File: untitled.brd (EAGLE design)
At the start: 100 x 80 mm, 31 parts, among them IC1 STM8S003F3

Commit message: second commit
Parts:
- added TP15: TPB2,54, testpad:B2,54
- moved SWIM 34.9 mm to (38.7, 11.7)
- moved TP13 29.6 mm to (27.3, 9.21)
- moved TP14 29.4 mm to (22.9, 9.21)
- moved C5 26.9 mm to (44.1, 15.6)
- moved IC1 24.5 mm to (38.7, 18.1)
- moved TP4 20.6 mm to (45.4, 24.1)
- moved TP3 20.3 mm to (45.4, 27.6)
- moved C2 11.1 mm to (38.1, 26.6)
- moved C4 11.1 mm to (40.3, 24.7)
- moved L1 11.1 mm to (42.5, 24.4)
- moved R4 11.1 mm to (37.1, 23.7)
- moved C3 11.1 mm to (41.3, 27.6)
- moved TP8 10.9 mm to (36.2, 30.8)
- moved TP6 9.74 mm to (36.2, 34.6)
- moved TP7 9.10 mm to (40.0, 30.8)
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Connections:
- removed net N$25: C1.2, C5.2, IC1.7, SWIM.3
- new net N$1: IC1.14, TP15.TP
- net GND: now also C1.2, C5.2, IC1.7, SWIM.3
- net NEXT: now also IC1.17; no longer IC1.1
- net PLAY_PAUSE: now also IC1.20; no longer IC1.3
- net PRE: now also IC1.19; no longer IC1.2
- net VOL+: now also IC1.15; no longer IC1.19
- net VOL-: now also IC1.16; no longer IC1.20
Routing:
- net LED0: track 48.8 -> 4.59 mm
- net VCC: track 43.8 -> 85.5 mm
- net VOL+: track 45.2 -> 5.72 mm
- net VOL-: track 41.7 -> 5.52 mm
- net PLAY_PAUSE: track 31.6 -> 4.76 mm
- net PRE: track 27.3 -> 5.41 mm
- net GND: track 77.5 -> 57.8 mm
- net NEXT: track 22.9 -> 5.33 mm
- net N$26: track 3.97 -> 9.89 mm
- net N$18: track 7.21 -> 12.6 mm
- net N$28: track 10.6 -> 6.02 mm
- net N$16: track 9.52 -> 14.0 mm
- net N$10: track 4.50 -> 8.57 mm
- net N$9: track 7.07 -> 11.1 mm
- net N$25: track 3.95 -> 0.00 mm
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
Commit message: third commit
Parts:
- removed TP1, TP2: TPB2,54, testpad:B2,54
- added SWIM1: (no value), con-lstb:MA04-1
- added U$2: MCP1825SOT-223-3, SteelCaveRobotics-Power:SOT-223
- LED1, LED2, LED3: device led:CHIP-LED0805 -> led:CHIPLED_0603
- moved TP11 7.73 mm to (12.4, 20.3)
- moved TP9 7.62 mm to (12.7, 25.4)
- moved TP13 7.31 mm to (20.0, 8.89)
- moved TP12 6.70 mm to (10.8, 17.5)
- moved TP10 5.85 mm to (10.8, 22.9)
- moved R5 5.75 mm to (15.2, 16.5)
- moved LED1 4.49 mm to (13.3, 32.4)
- moved TP15 4.46 mm to (47.9, 15.6)
- moved LED3 3.24 mm to (13.3, 29.8)
- moved TP14 2.88 mm to (25.7, 8.89)
- moved TP6 1.59 mm to (37.8, 34.6)
- moved TP8 1.59 mm to (37.8, 30.8)
- moved TP5 1.27 mm to (41.3, 34.6)
- moved TP7 1.27 mm to (41.3, 30.8)
- moved LED2 0.90 mm to (13.3, 31.1)
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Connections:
- removed net N$13: TP1.TP, U$1.P$10
- removed net N$14: TP2.TP, U$1.P$11
- new net VDD: TP13.TP, U$2.1
- net GND: now also U$2.2
- net LED0: now also LED3.C; no longer LED1.C
- net LED2: now also LED1.C; no longer LED3.C
- net N$1: now also IC1.3; no longer IC1.14
- net N$20: now also SWIM1.1
- net N$21: now also SWIM1.2
- net N$22: now also SWIM1.3
- net N$23: now also SWIM1.4
- net N$4: now also LED1.A; no longer LED3.A
- net N$6: now also LED3.A; no longer LED1.A
- net VCC: now also U$2.3; no longer TP13.TP
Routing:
- net N$12: track 14.3 -> 2.48 mm
- net VCC: track 85.5 -> 74.2 mm
- net N$14: track 9.00 -> 0.00 mm, vias 0 -> 1
- net N$1: track 0.00 -> 6.67 mm
- net N$13: track 6.39 -> 0.00 mm, vias 0 -> 1
- net VDD: track 0.00 -> 5.56 mm
- net N$15: track 12.0 -> 7.16 mm
- net GND: track 57.8 -> 62.3 mm
- net N$23: track 18.6 -> 14.6 mm
- net N$22: track 16.8 -> 13.3 mm
- net N$21: track 14.5 -> 11.9 mm
- net N$20: track 13.4 -> 11.3 mm
- net N$19: track 6.40 -> 7.99 mm
- net N$16: track 14.0 -> 15.6 mm
- net N$6: track 1.81 -> 3.27 mm
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- added copper zone on layer 1, net GND

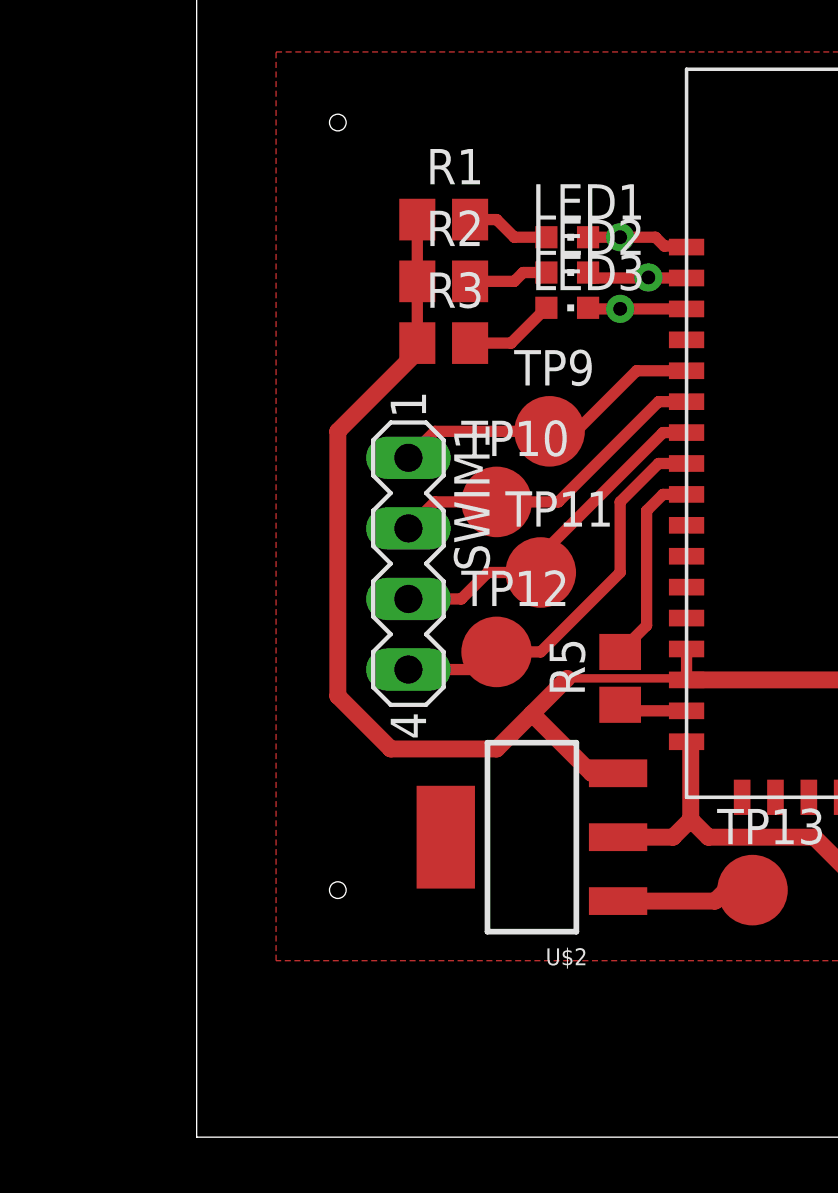
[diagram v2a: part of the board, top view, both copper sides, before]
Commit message: removed leds
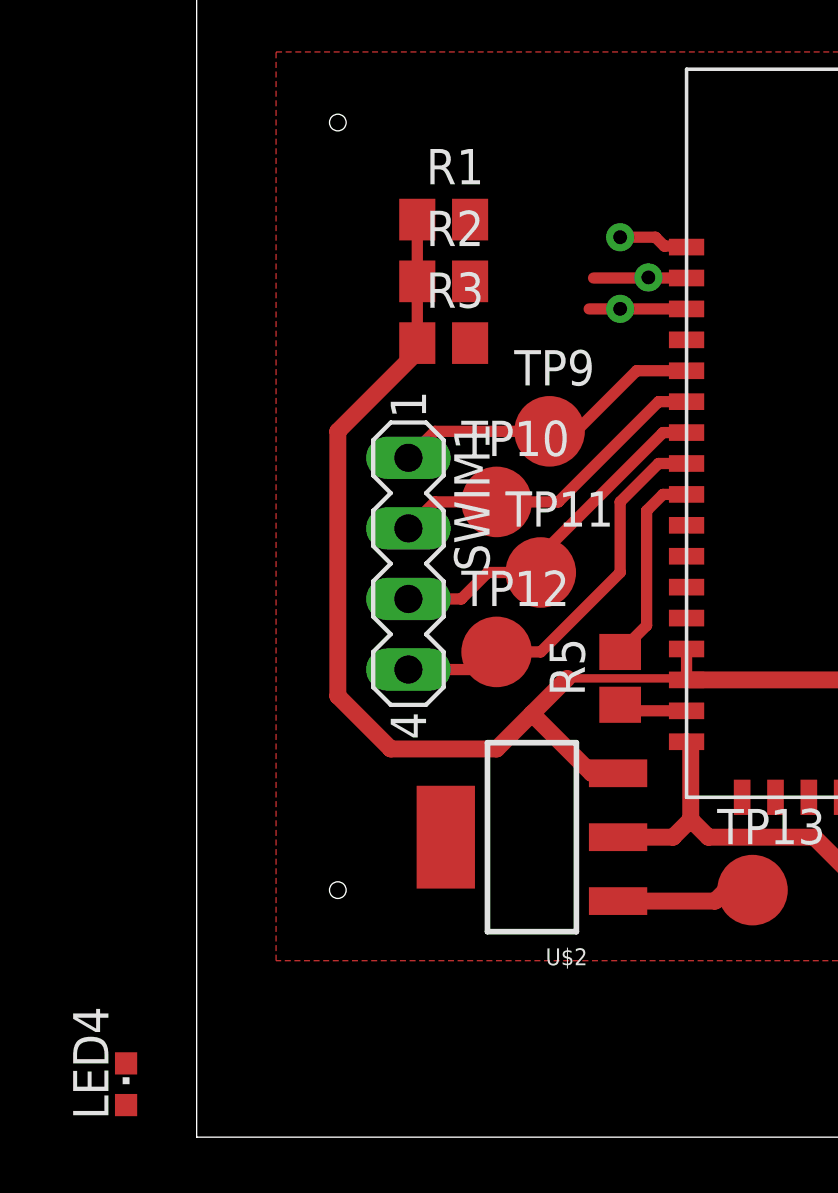
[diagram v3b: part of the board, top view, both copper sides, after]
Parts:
- removed LED1, LED2, LED3: (no value), led:CHIPLED_0603
- added LED4: (no value), led:CHIPLED_0603
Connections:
- removed net N$4: LED1.A, R1.2
- removed net N$5: LED2.A, R2.2
- removed net N$6: LED3.A, R3.2
- net LED0: now also R3.2; no longer LED3.C
- net LED1: now also R2.2; no longer LED2.C
- net LED2: now also R1.2; no longer LED1.C
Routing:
- net N$6: track 3.27 -> 0.00 mm
- net N$4: track 3.01 -> 0.00 mm
- net N$5: track 2.88 -> 0.00 mm
- net LED2: track 5.14 -> 3.98 mm
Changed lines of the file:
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@@
 <?xml version="1.0" encoding="utf-8"?>
 <!DOCTYPE eagle SYSTEM "eagle.dtd">
-<eagle version="7.3.0">
+<eagle version="7.4.0">
 <drawing>
 <settings>
@@
 <attribute name="OC_FARNELL" value="unknown" x="7.62" y="20.6375" size="1.778" layer="27" rot="R270" display="off"/>
 </element>
-<element name="LED1" library="led" package="CHIPLED_0603" value="" x="13.335" y="32.385" rot="R270"/>
-<element name="LED2" library="led" package="CHIPLED_0603" value="" x="13.335" y="31.115" rot="R270"/>
-<element name="LED3" library="led" package="CHIPLED_0603" value="" x="13.335" y="29.845" rot="R270"/>
 <element name="U$2" library="SteelCaveRobotics-Power" package="SOT-223" value="MCP1825SOT-223-3" x="12.065" y="10.795" rot="R90"/>
+<element name="LED4" library="led" package="CHIPLED_0603" value="" x="-2.54" y="1.905"/>
 </elements>
 <signals>
@@
 <wire x1="44.135" y1="18.415" x2="44.1325" y2="18.4175" width="0.4064" layer="1"/>
 </signal>
-<signal name="N$4">
-<contactref element="R1" pad="2"/>
-<contactref element="LED1" pad="A"/>
-<wire x1="12.585" y1="32.385" x2="11.43" y2="32.385" width="0.4064" layer="1"/>
-<wire x1="11.43" y1="32.385" x2="10.795" y2="33.02" width="0.4064" layer="1"/>
-<wire x1="10.795" y1="33.02" x2="9.84" y2="33.02" width="0.4064" layer="1"/>
-</signal>
-<signal name="N$5">
-<contactref element="R2" pad="2"/>
-<contactref element="LED2" pad="A"/>
-<wire x1="12.585" y1="31.115" x2="11.7475" y2="31.115" width="0.4064" layer="1"/>
-<wire x1="11.7475" y1="31.115" x2="11.43" y2="30.7975" width="0.4064" layer="1"/>
-<wire x1="11.43" y1="30.7975" x2="9.84" y2="30.7975" width="0.4064" layer="1"/>
-</signal>
-<signal name="N$6">
-<contactref element="R3" pad="2"/>
-<contactref element="LED3" pad="A"/>
-<wire x1="9.84" y1="28.575" x2="11.315" y2="28.575" width="0.4064" layer="1"/>
-<wire x1="11.315" y1="28.575" x2="12.585" y2="29.845" width="0.4064" layer="1"/>
-</signal>
 <signal name="VCC">
 <contactref element="R1" pad="1"/>
@@
 <contactref element="IC1" pad="10"/>
 <contactref element="U$1" pad="P$1"/>
-<contactref element="LED1" pad="C"/>
-<wire x1="14.085" y1="32.385" x2="15.24" y2="32.385" width="0.4064" layer="1"/>
 <wire x1="15.24" y1="32.385" x2="16.51" y2="32.385" width="0.4064" layer="1"/>
 <wire x1="16.51" y1="32.385" x2="16.8275" y2="32.0675" width="0.4064" layer="1"/>
@@
 <wire x1="41.6528" y1="21.0225" x2="42.295" y2="21.0225" width="0.4064" layer="1"/>
 <wire x1="42.295" y1="21.0225" x2="42.8625" y2="21.59" width="0.4064" layer="1"/>
+<contactref element="R1" pad="2"/>
 <wire x1="17.63" y1="32.03" x2="41.6528" y2="21.0225" width="0" layer="19" extent="1-1"/>
+<wire x1="9.84" y1="33.02" x2="15.24" y2="32.385" width="0" layer="19" extent="1-1"/>
 </signal>
 <signal name="LED1">
 <contactref element="IC1" pad="12"/>
 <contactref element="U$1" pad="P$2"/>
-<contactref element="LED2" pad="C"/>
 <wire x1="17.63" y1="30.9175" x2="14.2825" y2="30.9175" width="0.4064" layer="1"/>
-<wire x1="14.2825" y1="30.9175" x2="14.085" y2="31.115" width="0.4064" layer="1"/>
 <wire x1="35.8172" y1="20.3725" x2="34.8725" y2="20.3725" width="0.4064" layer="1"/>
 <wire x1="34.8725" y1="20.3725" x2="34.6075" y2="20.6375" width="0.4064" layer="1"/>
+<contactref element="R2" pad="2"/>
 <wire x1="17.63" y1="30.9175" x2="34.6075" y2="20.6375" width="0" layer="19" extent="1-1"/>
+<wire x1="9.84" y1="30.7975" x2="14.2825" y2="30.9175" width="0" layer="19" extent="1-1"/>
 </signal>
 <signal name="LED0">
 <contactref element="IC1" pad="11"/>
 <contactref element="U$1" pad="P$3"/>
-<contactref element="LED3" pad="C"/>
 <wire x1="17.63" y1="29.805" x2="14.125" y2="29.805" width="0.4064" layer="1"/>
-<wire x1="14.125" y1="29.805" x2="14.085" y2="29.845" width="0.4064" layer="1"/>
 <wire x1="35.8172" y1="21.0225" x2="35.4925" y2="21.0225" width="0.4064" layer="1"/>
 <wire x1="35.4925" y1="21.0225" x2="35.2425" y2="21.2725" width="0.4064" layer="1"/>
@@
 <wire x1="35.2425" y1="21.59" x2="35.56" y2="21.9075" width="0.4064" layer="1"/>
 <wire x1="35.56" y1="21.9075" x2="35.8775" y2="21.9075" width="0.4064" layer="1"/>
+<contactref element="R3" pad="2"/>
 <wire x1="17.63" y1="29.805" x2="35.2425" y2="21.59" width="0" layer="19" extent="1-1"/>
+<wire x1="9.84" y1="28.575" x2="14.125" y2="29.805" width="0" layer="19" extent="1-1"/>
 </signal>
 <signal name="N$1">

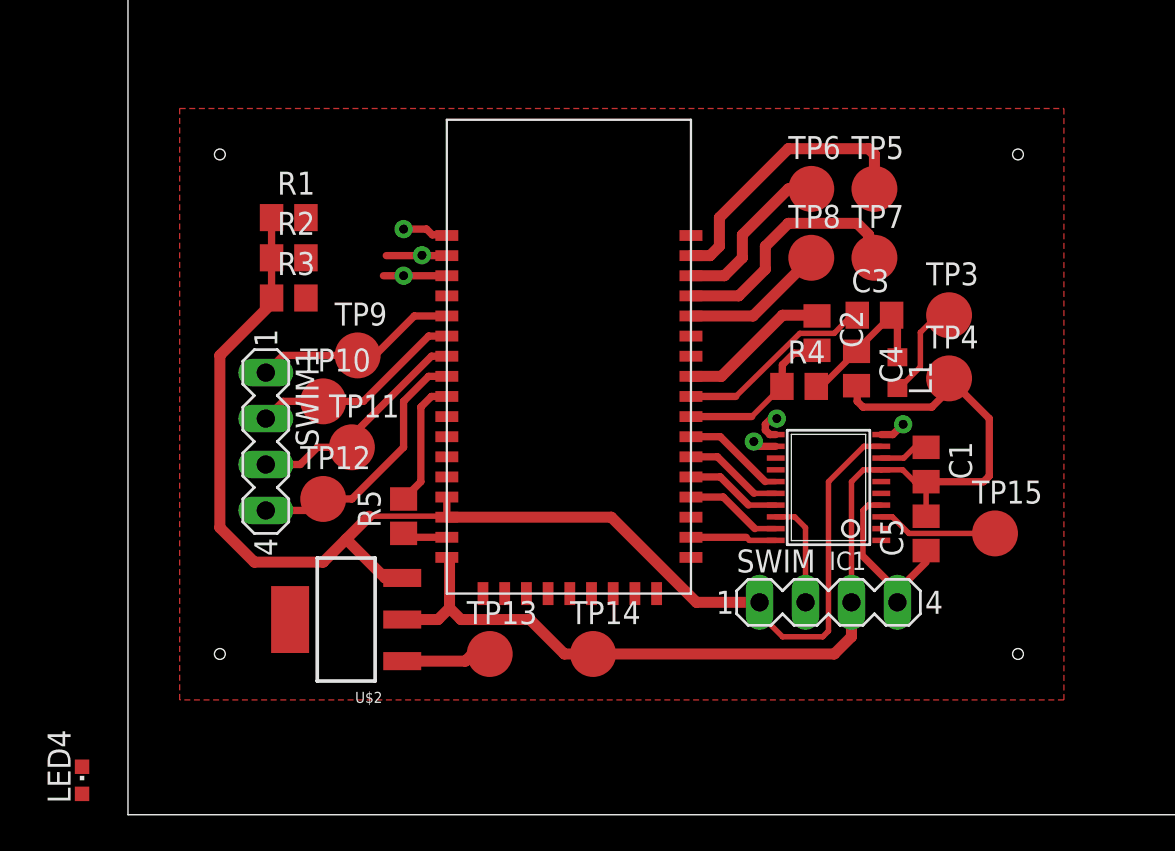
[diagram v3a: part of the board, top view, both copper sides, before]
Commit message: added tx signal + led
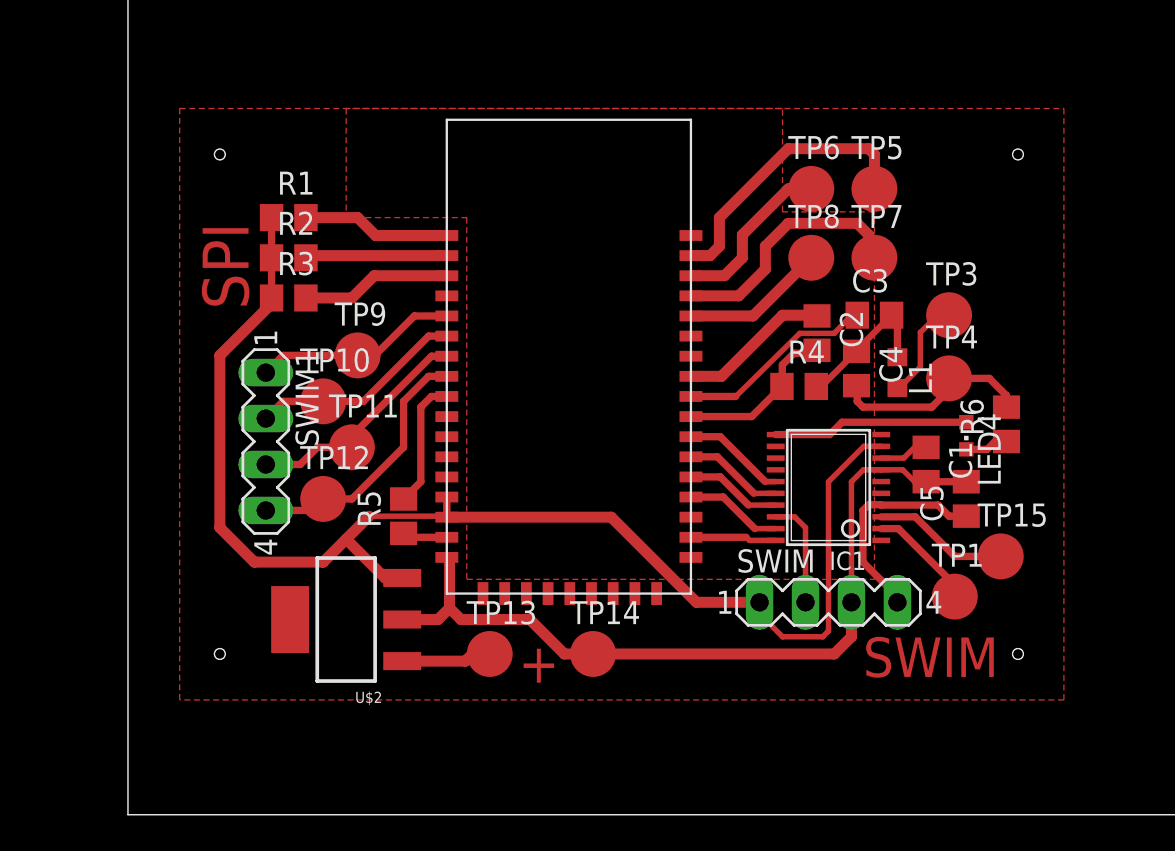
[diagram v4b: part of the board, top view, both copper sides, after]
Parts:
- added R6: 100, rcl:R0805
- added TP1: TPB2,54, testpad:B2,54
- moved LED4 52.5 mm to (46.4, 21.0), turned to 180 degrees
- moved C5 2.93 mm to (46.4, 17.5)
- moved TP15 1.31 mm to (48.3, 14.3)
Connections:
- new net N$29: LED4.C, R6.1
- new net N$5: IC1.2, TP1.TP
- new net N$6: IC1.11, LED4.A
- net GND: now also R6.2
- net LED0: now also IC1.10; no longer IC1.11
- net LED1: no longer IC1.12
- net LED2: no longer IC1.10
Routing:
- net N$6: track 0.00 -> 10.8 mm
- net N$5: track 0.00 -> 6.00 mm
- net GND: track 62.3 -> 57.3 mm
- net LED2: track 3.98 -> 8.20 mm, vias 1 -> 0
- net LED1: track 4.67 -> 7.84 mm
- net LED0: track 5.27 -> 8.30 mm
- net N$29: track 0.00 -> 2.40 mm
- net N$26: track 9.89 -> 12.0 mm
- net N$1: track 6.67 -> 7.51 mm
- added copper zone on layer 1, net N$4
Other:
- board text added: "+"
- board text added: "SPI"
- board text added: "SWIM"

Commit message: new design
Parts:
- removed TP10, TP11, TP12, TP9: TPB2,54, testpad:B2,54
- added C6, C7: 104, rcl:C0805
- added LED1: (no value), led:CHIPLED_0603
- added R10, R7, R8, R9: (no value), rcl:R0805
- moved SWIM1 0.71 mm to (7.94, 21.3)
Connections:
- new net N$30: R8.2, U$1.P$6
- new net N$31: R9.1, SWIM1.3
- new net N$32: R10.2, U$1.P$8
- new net N$33: R10.1, SWIM1.4
- new net N$34: LED1.C, U$1.P$2
- net GND: now also C6.2, C7.2
- net LED1: now also LED1.A; no longer U$1.P$2
- net N$20: now also R7.2; no longer SWIM1.1, TP9.TP
- net N$21: now also R7.1, SWIM1.1; no longer SWIM1.2, TP10.TP, U$1.P$6
- net N$22: now also R9.2; no longer SWIM1.3, TP11.TP
- net N$23: now also R8.1, SWIM1.2; no longer SWIM1.4, TP12.TP, U$1.P$8
- net VCC: now also C7.1
- net VDD: now also C6.1
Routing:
- net N$23: track 14.6 -> 3.97 mm
- net N$21: track 11.9 -> 3.84 mm
- net N$22: track 13.3 -> 5.91 mm
- net N$32: track 0.00 -> 7.12 mm
- net N$20: track 11.3 -> 4.99 mm
- net LED1: track 7.84 -> 1.96 mm
- net N$30: track 0.00 -> 5.45 mm
- net N$34: track 0.00 -> 4.55 mm
- net N$33: track 0.00 -> 4.23 mm
- net N$31: track 0.00 -> 4.10 mm
- net VCC: track 74.2 -> 76.3 mm
